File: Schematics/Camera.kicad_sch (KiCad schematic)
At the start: 7 parts, among them U3 TPS22917DBVR

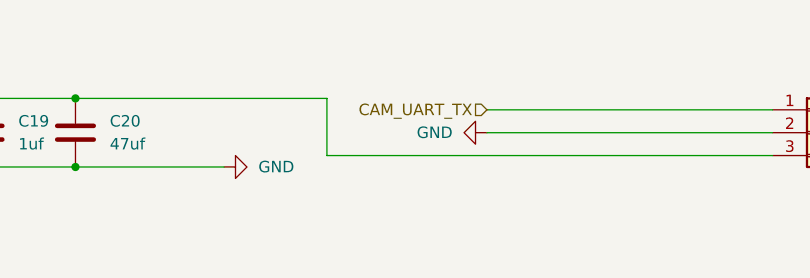
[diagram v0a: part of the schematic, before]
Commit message: dfm complete sent for order
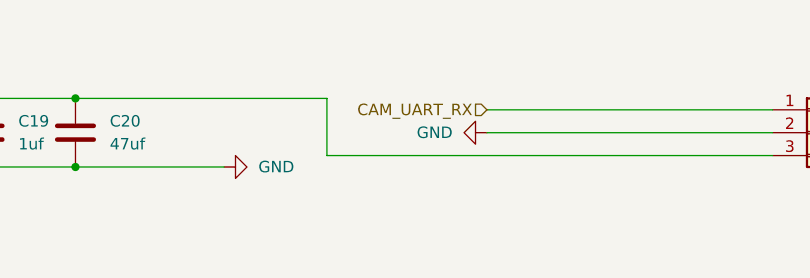
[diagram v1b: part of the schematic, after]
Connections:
- net CAM_UART_TX renamed CAM_UART_RX
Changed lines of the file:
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@@
 		)
 	)
-	(hierarchical_label "CAM_UART_TX"
+	(hierarchical_label "CAM_UART_RX"
 		(shape input)
 		(at 182.88 91.44 180)
